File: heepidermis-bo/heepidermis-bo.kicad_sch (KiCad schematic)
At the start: 1 part

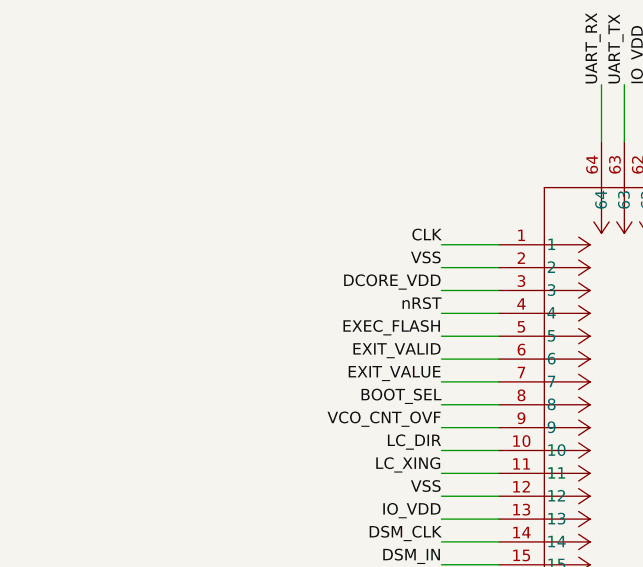
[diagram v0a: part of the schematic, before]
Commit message: Before re-routing programmer
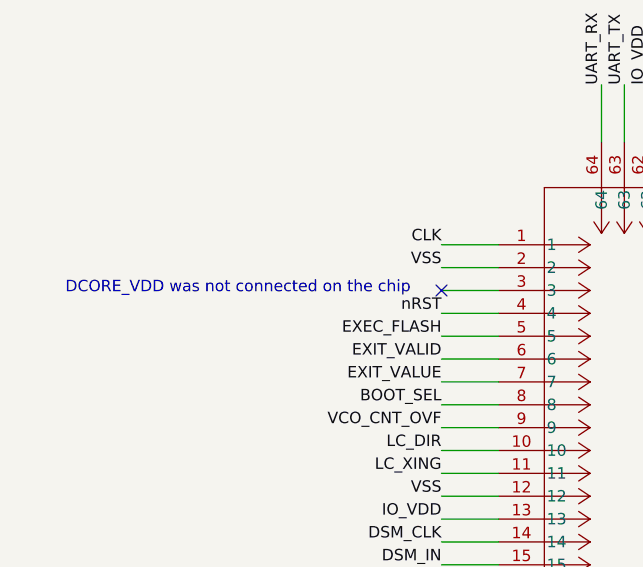
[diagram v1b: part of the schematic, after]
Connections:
- net DCORE_VDD: no longer HEEPidermis1.3
- no-connect marks 0 -> 1
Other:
- note added: "DCORE_VDD was not connected on the chip"
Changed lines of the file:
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@@
 	(generator_version "8.0")
 	(paper "A4")
+	(no_connect
+		(at 105.41 80.01)
+	)
 	(wire
 		(pts
@@
 			(width 0)
 			(type default)
+		)
+	)
+	(text "DCORE_VDD was not connected on the chip"
+		(exclude_from_sim no)
+		(at 82.804 79.756 0)
+		(effects
+			(font
+				(size 1.27 1.27)
+			)
 		)
 	)
@@
 		(effects
 			(font
-				(size 1.27 1.27)
-			)
-			(justify right bottom)
-		)
-	)
-	(label "DCORE_VDD"
-		(at 105.41 80.01 180)
-		(effects
-			(font

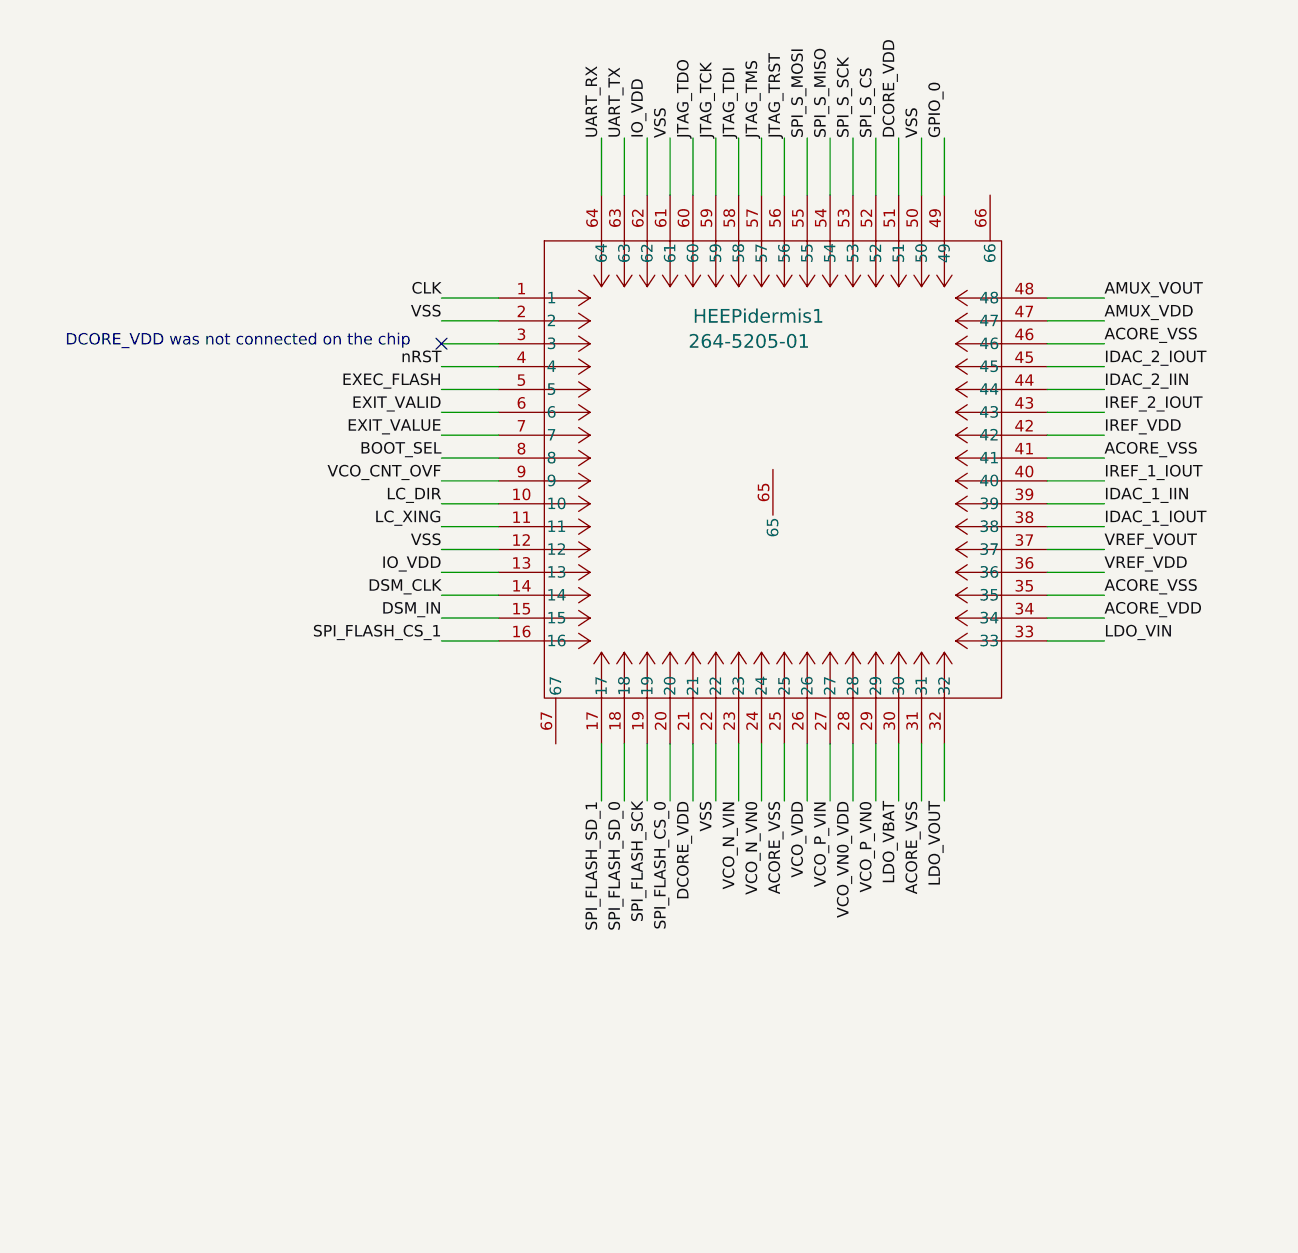
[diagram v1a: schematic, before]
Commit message: Routed all power signals and re-organized GPIOs
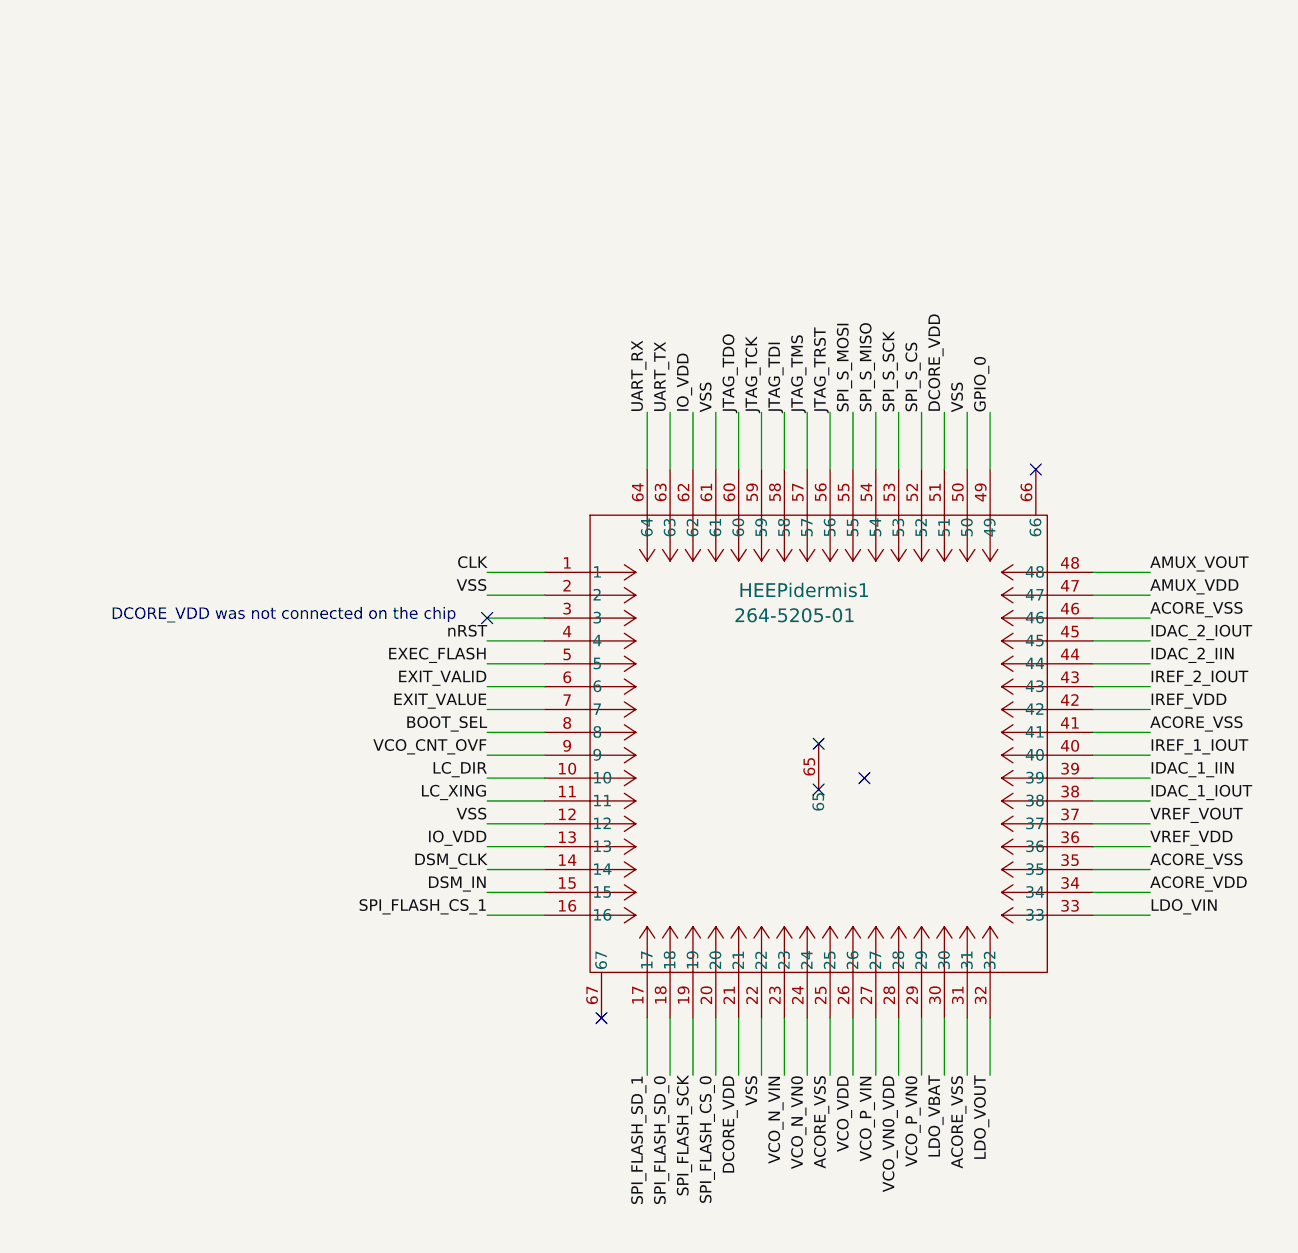
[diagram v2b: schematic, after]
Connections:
- no-connect marks 1 -> 6
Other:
- moved on the sheet: HEEPidermis1
